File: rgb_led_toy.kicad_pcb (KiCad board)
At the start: 2 copper layers, 43.4 x 43.4 mm, 31 parts, among them IC1 AT168, P1 I2C, P2 PORTC, P3 FTDI, U1 MADW__TSOP38238

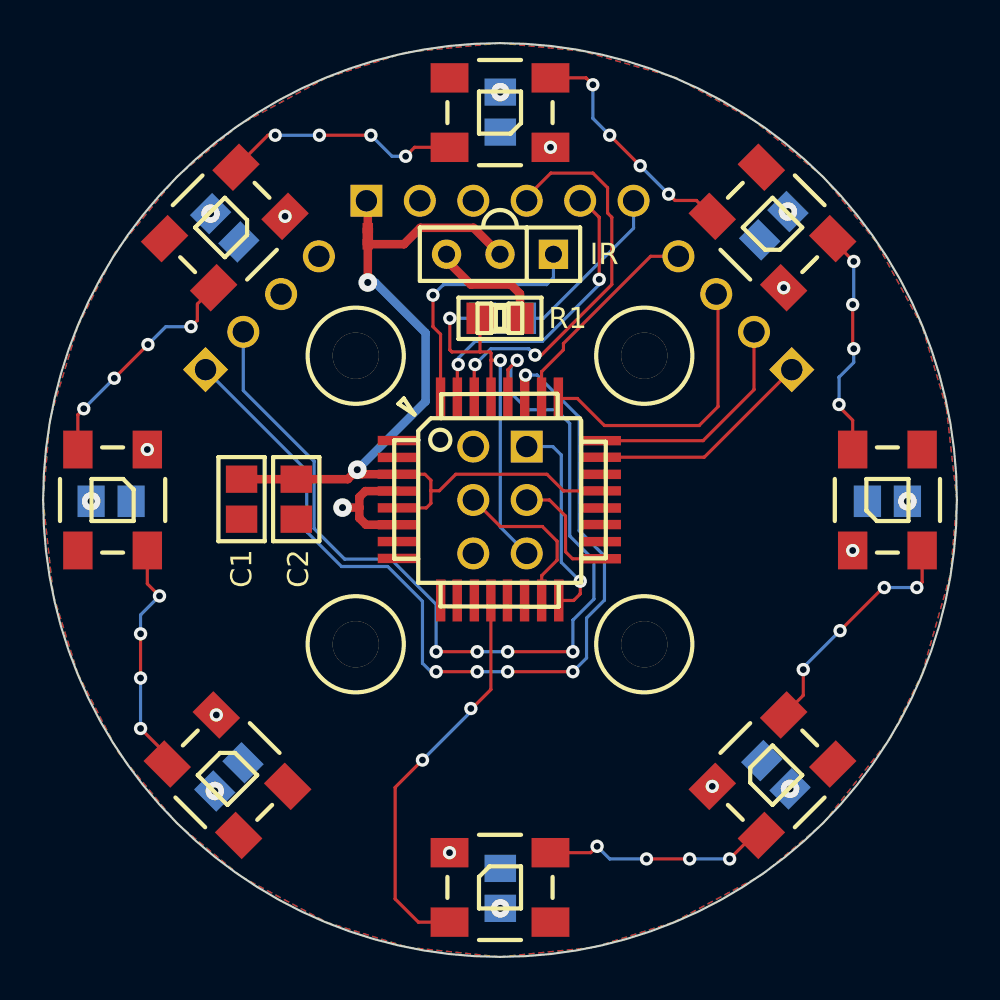
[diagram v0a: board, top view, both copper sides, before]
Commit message: LED-string now goes clockwise. Added 1.27mm headers for all MCU pins.
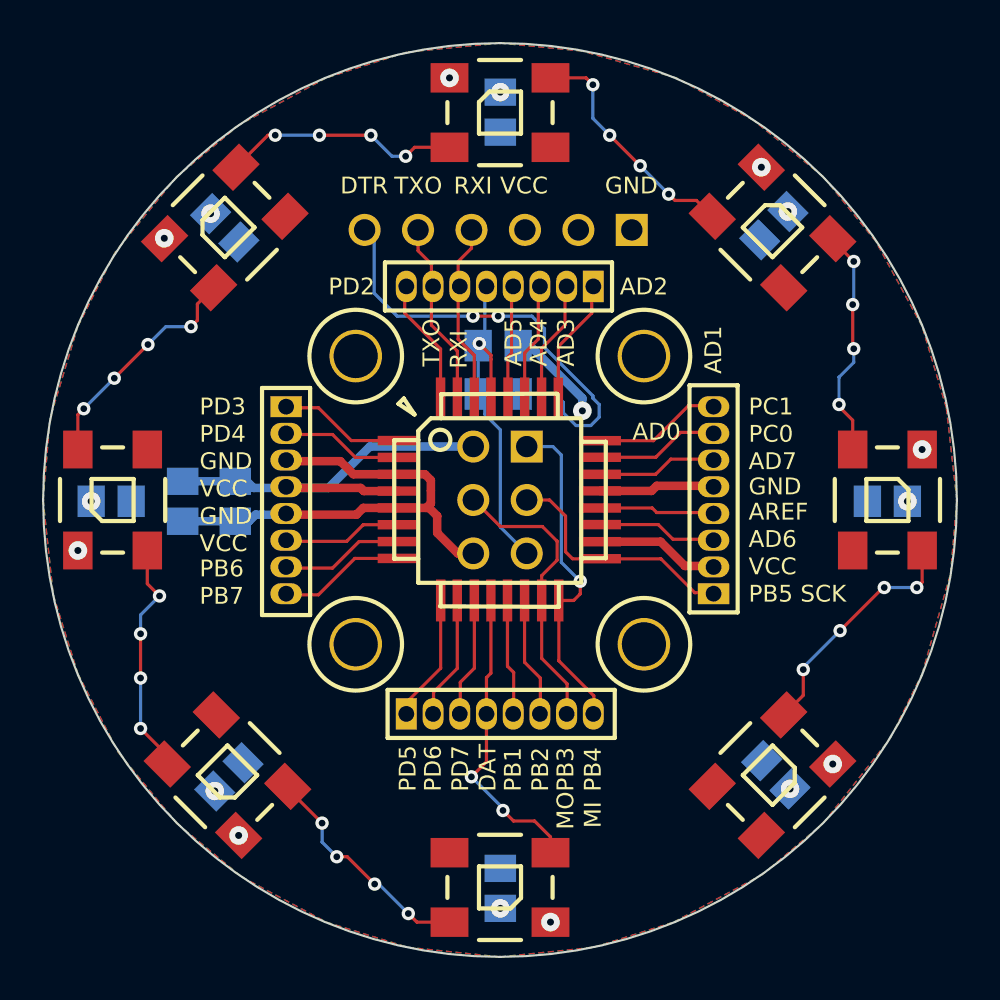
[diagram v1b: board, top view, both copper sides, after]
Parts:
- removed NJ1: NET-JOIN, MADW__SMD-net-noin-0.5mm
- removed U1: MADW__TSOP38238, SIL-3
- added G1: OSHW-logo_silkscreen_4mm, OSHW-logo_silkscreen_4mm, B.Cu at (71.8, 63.4)
- added G2: LED_smile_silkscreen_4mm, LED_smile_silkscreen_4mm, B.Cu at (94.6, 63.5)
- added P3: CONN_8, MADW__SIL-8-1.27mm, F.Cu at (93.3, 70.7)
- added P4: CONN_8, MADW__SIL-8-1.27mm, F.Cu at (83.2, 60.6)
- C1, C2, R1: moved to B.Cu
- IC1: value AT168 -> ATMEGA328-A
- MH1, MH2, MH3, MH4: footprint MADW__mounting_hole_3mm -> MADW__mounting_hole_2mm
- P1: value I2C -> CONN_8; footprint MADW__SIL-4 -> MADW__SIL-8-1.27mm; moved to F.Cu
- P2: value PORTC -> CONN_8; footprint MADW__SIL-4 -> MADW__SIL-8-1.27mm; moved to F.Cu
- moved P2 22.1 mm to (83.2, 80.9), turned to 0 degrees
- moved P1 8.97 mm to (73.0, 70.7), turned to 270 degrees
- moved C2 5.40 mm to (68.1, 70.8), turned to 270 degrees
- moved C3 3.61 mm to (83.1, 65.7)
- moved P5 1.39 mm to (83.1, 57.9), turned to 180 degrees
- moved R1 1.30 mm to (83.1, 63.4)
- moved C1 0.32 mm to (70.6, 70.8), turned to 270 degrees
- turned LED1 to 90 degrees
- turned LED2 to 45 degrees
- turned LED3 to 0 degrees
- turned LED4 to 315 degrees
- turned LED5 to 270 degrees
- turned LED6 to 225 degrees
- turned LED7 to 180 degrees
- turned LED8 to 135 degrees
- renumbered LED8 to LED2, LED7 to LED3, LED6 to LED4, LED4 to LED6, LED3 to LED7, LED2 to LED8, P3 to P5
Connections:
- C10 pad 2: GNDPWR -> GND
- C11 pad 2: GNDPWR -> GND
- C4 pad 2: GNDPWR -> GND
- C5 pad 2: GNDPWR -> GND
- C6 pad 2: GNDPWR -> GND
- C7 pad 2: GNDPWR -> GND
- C8 pad 2: GNDPWR -> GND
- C9 pad 2: GNDPWR -> GND
- IC1 pad 1: (no net) -> /PD3
- IC1 pad 10: (no net) -> /PD6
- IC1 pad 11: (no net) -> /PD7
- IC1 pad 13: (no net) -> /PB1
- IC1 pad 14: (no net) -> /PB2
- IC1 pad 19: (no net) -> /ADC6
- IC1 pad 2: (no net) -> /PD4
- IC1 pad 20: (no net) -> /AREF
- IC1 pad 22: (no net) -> /ADC7
- IC1 pad 27: /SDA -> /PC4
- IC1 pad 28: /SCL -> /PC5
- IC1 pad 32: /INT0 -> /PD2
- IC1 pad 7: (no net) -> /PB6
- IC1 pad 8: (no net) -> /PB7
- IC1 pad 9: (no net) -> /PD5
- JP1 pad 6: GNDPWR -> GND
- LED1 pad 2: N-000006 -> N-0000034
- LED1 pad 3: GNDPWR -> GND
- LED2 pad 2: (no net) -> N-0000037
- LED2 pad 3: GNDPWR -> GND
- LED2 pad 4: N-000001 -> N-0000034
- LED3 pad 2: N-000001 -> N-0000041
- LED3 pad 3: GNDPWR -> GND
- LED3 pad 4: N-000008 -> N-0000037
- LED4 pad 2: N-000008 -> N-0000038
- LED4 pad 3: GNDPWR -> GND
- LED4 pad 4: N-000009 -> N-0000041
- LED5 pad 2: N-000009 -> N-0000042
- LED5 pad 3: GNDPWR -> GND
- LED5 pad 4: N-000003 -> N-0000038
- LED6 pad 2: N-000003 -> N-0000040
- LED6 pad 3: GNDPWR -> GND
- LED6 pad 4: N-000005 -> N-0000042
- LED7 pad 2: N-000005 -> N-0000039
- LED7 pad 3: GNDPWR -> GND
- LED7 pad 4: N-000007 -> N-0000040
- LED8 pad 2: N-000007 -> (no net)
- LED8 pad 3: GNDPWR -> GND
- LED8 pad 4: N-000006 -> N-0000039
- P1 pad 1: /SDA -> /PD3
- P1 pad 2: /SCL -> /PD4
- P1 pad 3: GNDPWR -> GND
- P2 pad 1: /PC0 -> /PD5
- P2 pad 2: /PC1 -> /PD6
- P2 pad 3: /PC2 -> /PD7
- P2 pad 4: /PC3 -> /DATA
- P5 pad 1: GNDPWR -> GND
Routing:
- net /SCL: track 45.7 -> 0.00 mm, vias 5 -> 0
- net /SDA: track 44.9 -> 0.00 mm, vias 5 -> 0
- net VCC: track 11.8 -> 36.5 mm
- net /DTR: track 8.36 -> 22.2 mm, vias 0 -> 2
- net /INT0: track 12.2 -> 0.00 mm, vias 1 -> 0
- net N-000007: track 11.7 -> 0.00 mm, vias 4 -> 0
- net N-0000039: track 0.00 -> 11.7 mm, vias 0 -> 4
- net N-000009: track 11.4 -> 0.00 mm, vias 4 -> 0
- net N-0000038: track 0.00 -> 11.4 mm, vias 0 -> 4
- net N-0000042: track 0.00 -> 11.4 mm, vias 0 -> 4
- net N-000003: track 11.4 -> 0.00 mm, vias 4 -> 0
- net N-0000037: track 0.00 -> 11.3 mm, vias 0 -> 4
- net N-000001: track 11.3 -> 0.00 mm, vias 4 -> 0
- net N-000008: track 11.1 -> 0.00 mm, vias 4 -> 0
- net N-0000041: track 0.00 -> 11.1 mm, vias 0 -> 4
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- added copper zone on B.Cu, net GND
- removed copper zone on B.Cu, net GNDPWR
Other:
- board text added: "2013 V3.0.b"
- board text added: "AD0"
- board text added: "AD1"
- board text added: "AD2"
- board text added: "AD3"
- board text added: "AD4"
- board text added: "AD5"
- board text added: "AD6"
- board text added: "AD7"
- board text added: "AREF"
- board text added: "DAT"
- board text added: "FTDI"
- board text added: "ISP"
- board text added: "MI"
- board text added: "MO"
- board text added: "PB1"
- board text added: "PB2"
- board text added: "PB3"
- board text added: "PB4"
- board text added: "PB5 SCK"
- board text added: "PB6"
- board text added: "PB7"
- board text added: "PD2"
- board text added: "PD3"
- board text added: "PD4"
- board text added: "PD5"
- board text added: "PD6"
- board text added: "PD7"
- board text removed: "2013 V3.0.a"
- board text removed: "IR"
- board text removed: "NC"
- board text removed: "PC2"
- board text removed: "PC3"
- board text removed: "SCL"
- board text removed: "SDA"

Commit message: Tweaks: silkscreen, copper p. cutouts, 8mil min trace width, 16MHz reso.
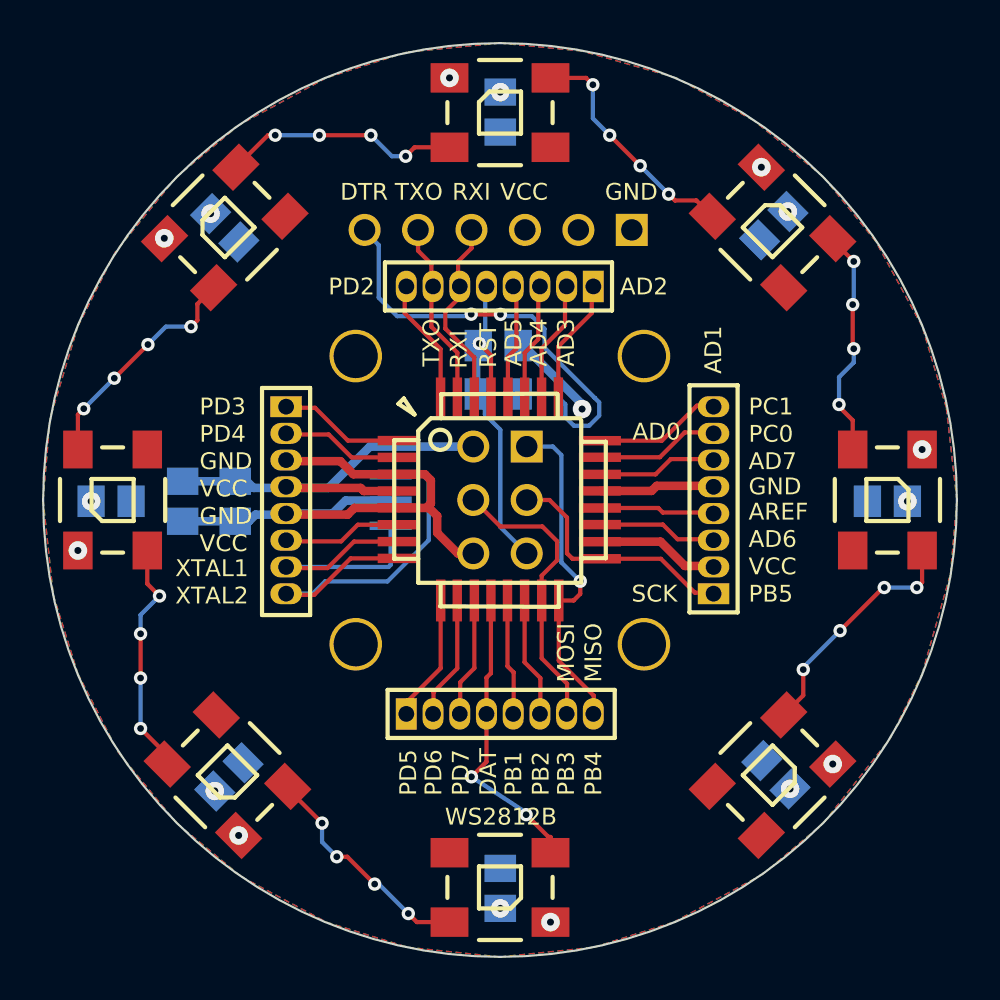
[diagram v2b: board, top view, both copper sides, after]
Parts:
- added Q1: 16MHz, MADW__murata-resonator_CSTCE-G, B.Cu at (78.0, 70.8)
- turned G1 to 180 degrees
- turned G2 to 180 degrees
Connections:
- net /PB6 renamed /XTAL1
- net /PB7 renamed /XTAL2
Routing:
- net /XTAL2: track 5.99 -> 18.6 mm
- net /XTAL1: track 5.79 -> 12.7 mm
- net GND: track 31.1 -> 36.3 mm
- net /RXI: track 8.59 -> 9.24 mm
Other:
- net class Default: clearance 0.1524 -> 0.2032; trace_width 0.1524 -> 0.2032
- net class LED removed
- net class POWER: clearance 0.1524 -> 0.2032
- rule trace_clearance: 0.1524 -> 0.2032
- rule trace_min: 0.1524 -> 0.2032
- board text added: "MISO"
- board text added: "MOSI"
- board text added: "PB5"
- board text added: "RST"
- board text added: "SCK"
- board text added: "WS2812B"
- board text added: "XTAL1"
- board text added: "XTAL2"
- board text added: "black"
- board text added: "green"
- board text removed: "MI"
- board text removed: "MO"
- board text removed: "PB5 SCK"
- board text removed: "PB6"
- board text removed: "PB7"

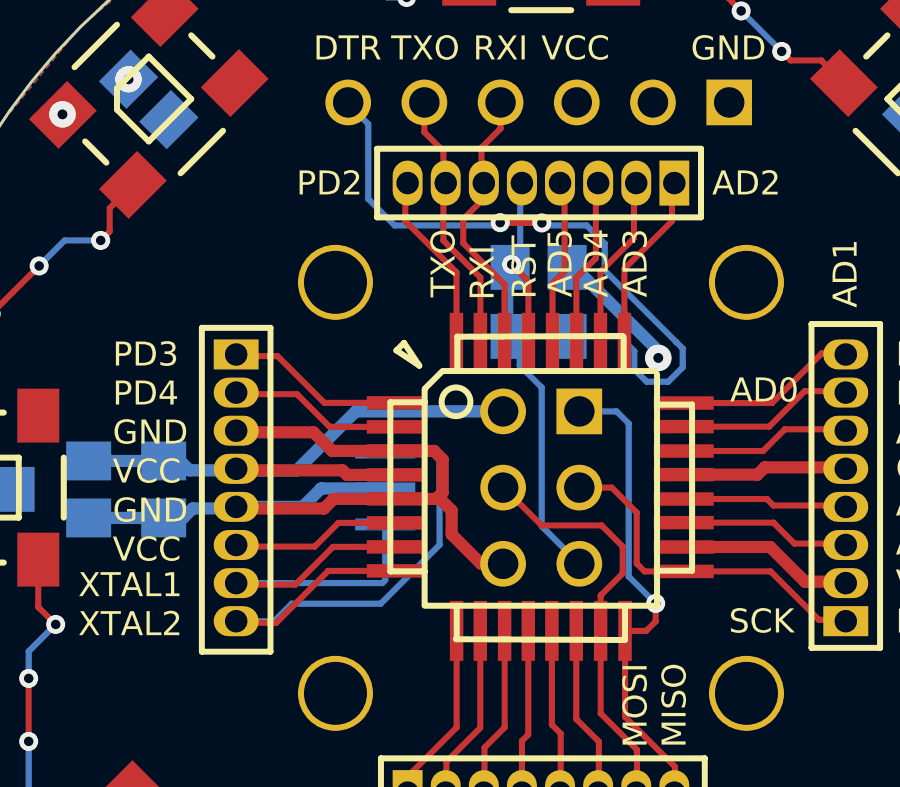
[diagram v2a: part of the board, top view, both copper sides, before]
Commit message: Had to fix the resonator footprint (library part was off).
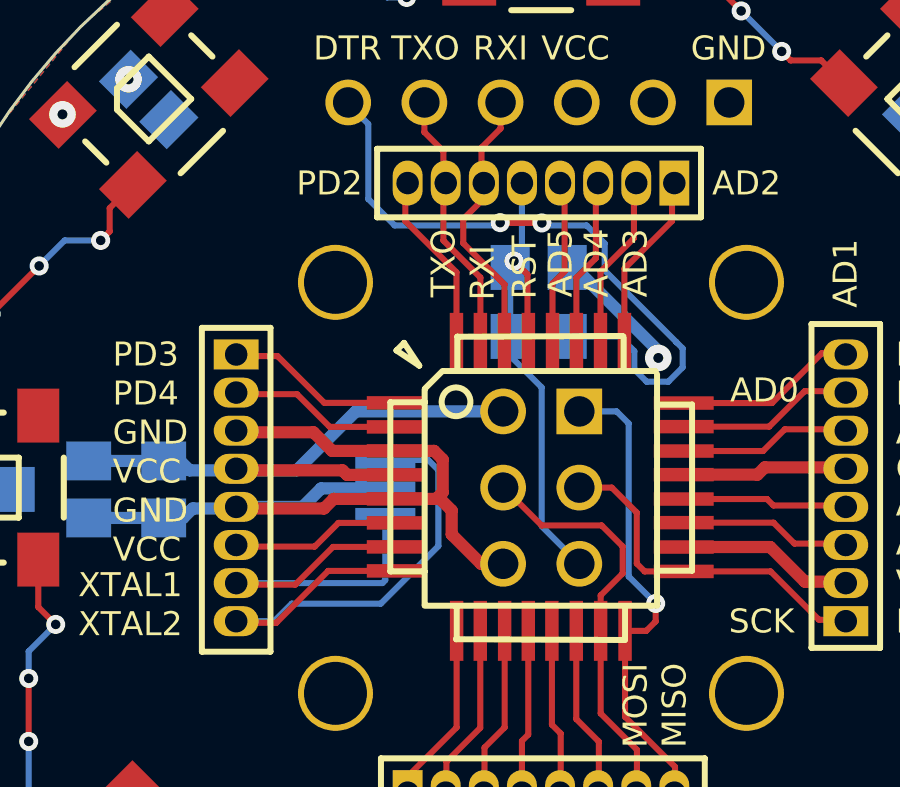
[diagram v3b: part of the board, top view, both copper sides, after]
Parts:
- Q1: value 16MHz -> CSTCE16M0V53-R0; footprint MADW__murata-resonator_CSTCE-G -> MADW__murata-resonator__CSTCE16M0V53-R0
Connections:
- net N-0000034 renamed Net-<LED2-Pad2>
- net N-0000035 renamed Net-<LED1-Pad2>
- net N-0000038 renamed Net-<LED4-Pad2>
- net N-0000039 renamed Net-<LED7-Pad2>
- net N-0000040 renamed Net-<LED6-Pad2>
- net N-0000041 renamed Net-<LED3-Pad2>
- net N-0000042 renamed Net-<LED5-Pad2>
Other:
- board text added: "2013 V3.0.c"
- board text removed: "2013 V3.0.b"
